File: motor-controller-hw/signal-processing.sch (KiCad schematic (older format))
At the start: 0 parts

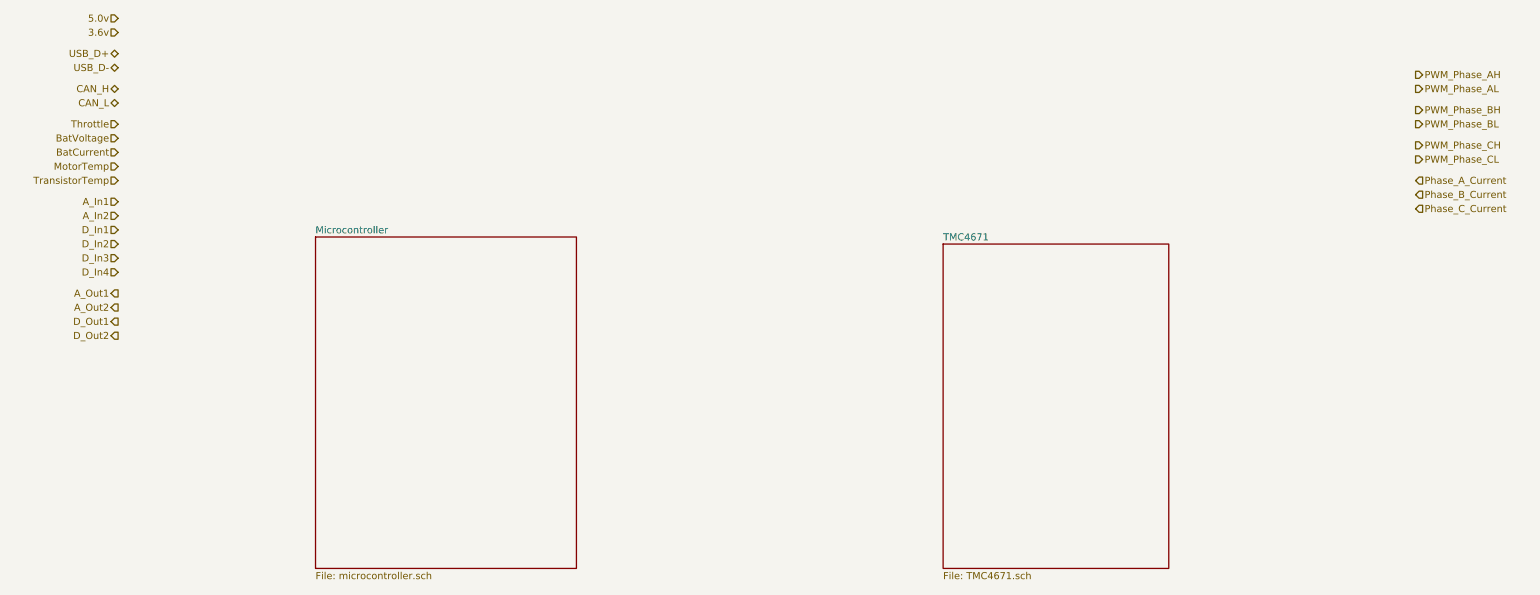
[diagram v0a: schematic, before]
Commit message: Added more signals to the top level diagram
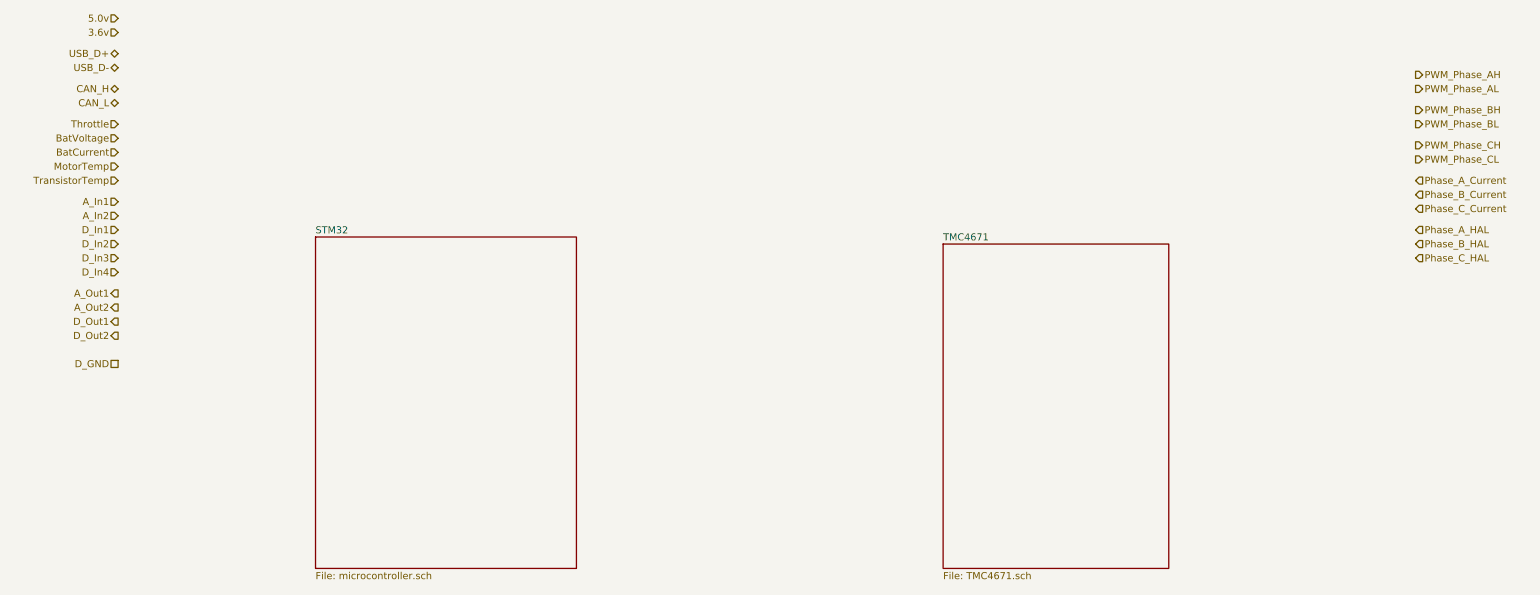
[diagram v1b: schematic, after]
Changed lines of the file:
@@
 S 2550 2350 1850 2350
 U 5BAADA91
-F0 "Microcontroller" 50
+F0 "STM32" 50
 F1 "microcontroller.sch" 50
 $EndSheet
@@
 Text HLabel 10350 2150 2    50   Input ~ 0
 Phase_C_Current
+Text HLabel 10350 2300 2    50   Input ~ 0
+Phase_A_HAL
+Text HLabel 10350 2400 2    50   Input ~ 0
+Phase_B_HAL
+Text HLabel 10350 2500 2    50   Input ~ 0
+Phase_C_HAL
+Text HLabel 1150 3250 0    50   UnSpc ~ 0
+D_GND
 $EndSCHEMATC

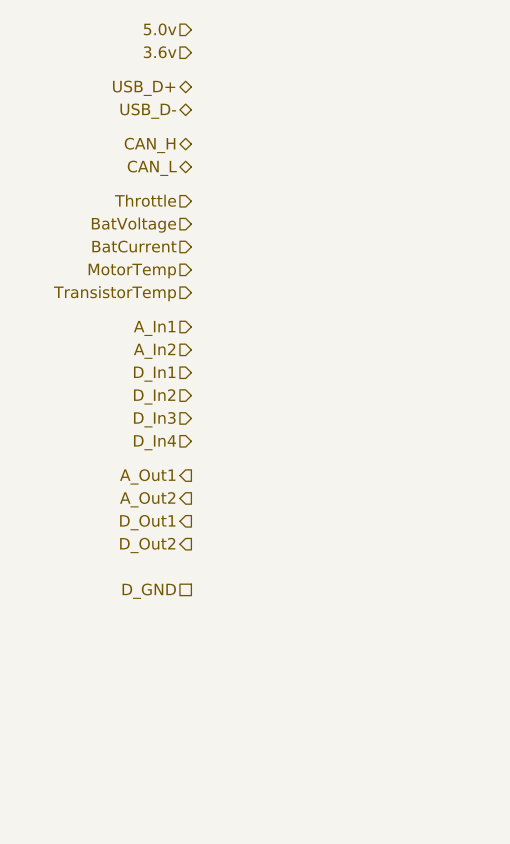
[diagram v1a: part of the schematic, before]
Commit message: added more signals and parts
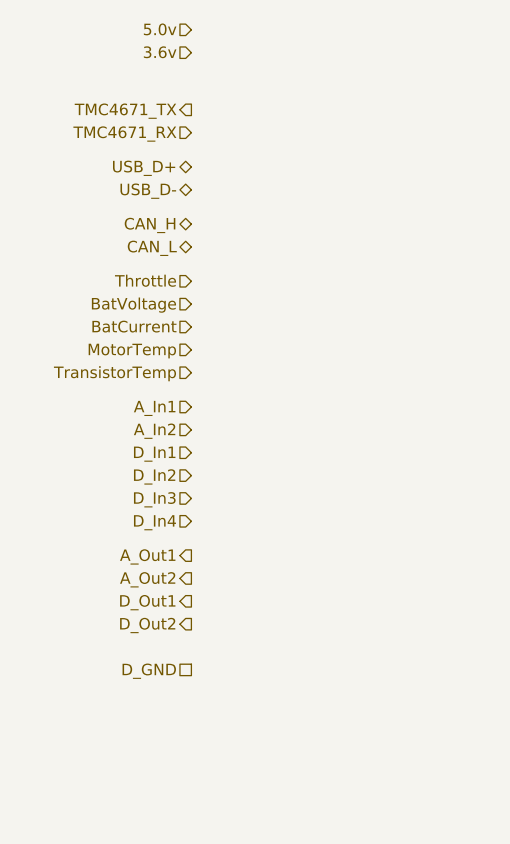
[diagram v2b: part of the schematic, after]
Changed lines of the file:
@@
 Text HLabel 1150 800  0    50   Input ~ 0
 5.0v
-Text HLabel 1150 1050 0    50   BiDi ~ 0
+Text HLabel 1150 1400 0    50   BiDi ~ 0
 USB_D+
-Text HLabel 1150 1150 0    50   BiDi ~ 0
+Text HLabel 1150 1500 0    50   BiDi ~ 0
 USB_D-
-Text HLabel 1150 1300 0    50   BiDi ~ 0
+Text HLabel 1150 1650 0    50   BiDi ~ 0
 CAN_H
-Text HLabel 1150 1400 0    50   BiDi ~ 0
+Text HLabel 1150 1750 0    50   BiDi ~ 0
 CAN_L
-Text HLabel 1150 1550 0    50   Input ~ 0
+Text HLabel 1150 1900 0    50   Input ~ 0
 Throttle
-Text HLabel 1150 1650 0    50   Input ~ 0
+Text HLabel 1150 2000 0    50   Input ~ 0
 BatVoltage
-Text HLabel 1150 1750 0    50   Input ~ 0
+Text HLabel 1150 2100 0    50   Input ~ 0
 BatCurrent
-Text HLabel 1150 1850 0    50   Input ~ 0
+Text HLabel 1150 2200 0    50   Input ~ 0
 MotorTemp
-Text HLabel 1150 1950 0    50   Input ~ 0
+Text HLabel 1150 2300 0    50   Input ~ 0
 TransistorTemp
-Text HLabel 1150 2100 0    50   Input ~ 0
+Text HLabel 1150 2450 0    50   Input ~ 0
 A_In1
-Text HLabel 1150 2200 0    50   Input ~ 0
+Text HLabel 1150 2550 0    50   Input ~ 0
 A_In2
-Text HLabel 1150 2300 0    50   Input ~ 0
+Text HLabel 1150 2650 0    50   Input ~ 0
 D_In1
-Text HLabel 1150 2400 0    50   Input ~ 0
+Text HLabel 1150 2750 0    50   Input ~ 0
 D_In2
-Text HLabel 1150 2500 0    50   Input ~ 0
+Text HLabel 1150 2850 0    50   Input ~ 0
 D_In3
-Text HLabel 1150 2600 0    50   Input ~ 0
+Text HLabel 1150 2950 0    50   Input ~ 0
 D_In4
-Text HLabel 1150 2750 0    50   Output ~ 0
+Text HLabel 1150 3100 0    50   Output ~ 0
 A_Out1
-Text HLabel 1150 2850 0    50   Output ~ 0
+Text HLabel 1150 3200 0    50   Output ~ 0
 A_Out2
-Text HLabel 1150 2950 0    50   Output ~ 0
+Text HLabel 1150 3300 0    50   Output ~ 0
 D_Out1
-Text HLabel 1150 3050 0    50   Output ~ 0
+Text HLabel 1150 3400 0    50   Output ~ 0
 D_Out2
 Text HLabel 10350 1200 2    50   Output ~ 0
@@
 Text HLabel 10350 2500 2    50   Input ~ 0
 Phase_C_HAL
-Text HLabel 1150 3250 0    50   UnSpc ~ 0
+Text HLabel 1150 3600 0    50   UnSpc ~ 0
 D_GND
+Text HLabel 1150 1250 0    50   Input ~ 0
+TMC4671_RX
+Text HLabel 1150 1150 0    50   Output ~ 0
+TMC4671_TX
 $EndSCHEMATC

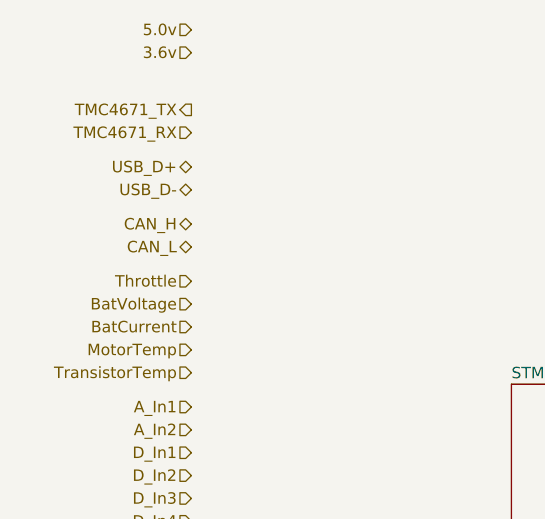
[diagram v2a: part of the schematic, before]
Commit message: Changed hierarchy Added input protection circuitry
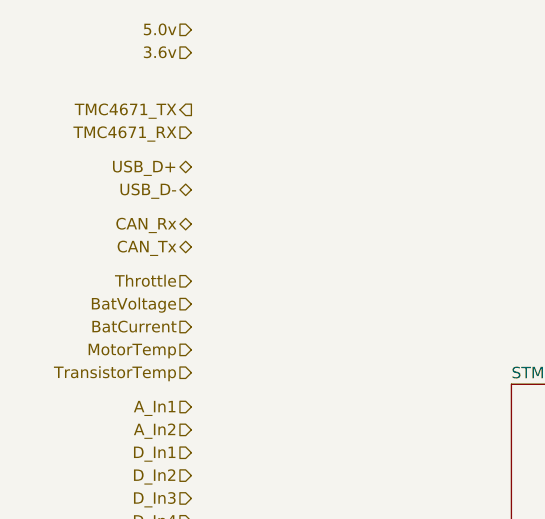
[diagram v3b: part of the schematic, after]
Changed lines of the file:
@@
 $Descr A4 11693 8268
 encoding utf-8
-Sheet 2 7
+Sheet 2 8
 Title ""
 Date ""
@@
 USB_D-
 Text HLabel 1150 1650 0    50   BiDi ~ 0
-CAN_H
+CAN_Rx
 Text HLabel 1150 1750 0    50   BiDi ~ 0
-CAN_L
+CAN_Tx
 Text HLabel 1150 1900 0    50   Input ~ 0
 Throttle
